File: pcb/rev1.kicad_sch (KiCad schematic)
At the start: 50 parts, among them SW1 SW_Push, SW10 SW_Push, SW11 SW_Push, SW12 SW_Push, SW13 SW_Push, SW14 SW_Push, SW15 SW_Push, SW16 SW_Push, SW2 SW_Push, SW3 SW_Push, SW4 SW_Push, SW5 SW_Push, SW6 SW_Push, SW7 SW_Push, SW8 SW_Push, SW9 SW_Push, U1 XIAO-RP2040-DIP, U2 OLED_0.91_128x32

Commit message: Fixed LED footprint
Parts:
- D1, D10, D11, D12, D13, D14, D15, D16, D2, D3, D4, D5, D6, D7, D8, D9: footprint LED_SMD:LED_SK6812_PLCC4_5.0x5.0mm_P3.2mm -> Hackclub symbols:MX_SK6812MINI-E_REV
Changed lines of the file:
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@@
 			)
 		)
-		(property "Footprint" "LED_SMD:LED_SK6812_PLCC4_5.0x5.0mm_P3.2mm"
+		(property "Footprint" "Hackclub symbols:MX_SK6812MINI-E_REV"
 			(at 67.31 128.27 0)
 			(effects
@@
 			)
 		)
-		(property "Footprint" "LED_SMD:LED_SK6812_PLCC4_5.0x5.0mm_P3.2mm"
+		(property "Footprint" "Hackclub symbols:MX_SK6812MINI-E_REV"
 			(at 102.87 146.05 0)
 			(effects
@@
 			)
 		)
-		(property "Footprint" "LED_SMD:LED_SK6812_PLCC4_5.0x5.0mm_P3.2mm"
+		(property "Footprint" "Hackclub symbols:MX_SK6812MINI-E_REV"
 			(at 85.09 146.05 0)
 			(effects
@@
 			)
 		)
-		(property "Footprint" "LED_SMD:LED_SK6812_PLCC4_5.0x5.0mm_P3.2mm"
+		(property "Footprint" "Hackclub symbols:MX_SK6812MINI-E_REV"
 			(at 120.65 146.05 0)
 			(effects
@@
 			)
 		)
-		(property "Footprint" "LED_SMD:LED_SK6812_PLCC4_5.0x5.0mm_P3.2mm"
+		(property "Footprint" "Hackclub symbols:MX_SK6812MINI-E_REV"
 			(at 120.65 128.27 0)
 			(effects
@@
 			)
 		)
-		(property "Footprint" "LED_SMD:LED_SK6812_PLCC4_5.0x5.0mm_P3.2mm"
+		(property "Footprint" "Hackclub symbols:MX_SK6812MINI-E_REV"
 			(at 102.87 163.83 0)
 			(effects
@@
 			)
 		)
-		(property "Footprint" "LED_SMD:LED_SK6812_PLCC4_5.0x5.0mm_P3.2mm"
+		(property "Footprint" "Hackclub symbols:MX_SK6812MINI-E_REV"
 			(at 85.09 110.49 0)
 			(effects
@@
 			)
 		)
-		(property "Footprint" "LED_SMD:LED_SK6812_PLCC4_5.0x5.0mm_P3.2mm"
+		(property "Footprint" "Hackclub symbols:MX_SK6812MINI-E_REV"
 			(at 67.31 110.49 0)
 			(effects
@@
 			)
 		)
-		(property "Footprint" "LED_SMD:LED_SK6812_PLCC4_5.0x5.0mm_P3.2mm"
+		(property "Footprint" "Hackclub symbols:MX_SK6812MINI-E_REV"
 			(at 120.65 110.49 0)
 			(effects
@@
 			)
 		)
-		(property "Footprint" "LED_SMD:LED_SK6812_PLCC4_5.0x5.0mm_P3.2mm"
+		(property "Footprint" "Hackclub symbols:MX_SK6812MINI-E_REV"
 			(at 67.31 163.83 0)
 			(effects
@@
 			)
 		)
-		(property "Footprint" "LED_SMD:LED_SK6812_PLCC4_5.0x5.0mm_P3.2mm"
+		(property "Footprint" "Hackclub symbols:MX_SK6812MINI-E_REV"
 			(at 102.87 128.27 0)
 			(effects
@@
 			)
 		)
-		(property "Footprint" "LED_SMD:LED_SK6812_PLCC4_5.0x5.0mm_P3.2mm"
+		(property "Footprint" "Hackclub symbols:MX_SK6812MINI-E_REV"
 			(at 102.87 110.49 0)
 			(effects
@@
 			)
 		)
-		(property "Footprint" "LED_SMD:LED_SK6812_PLCC4_5.0x5.0mm_P3.2mm"
+		(property "Footprint" "Hackclub symbols:MX_SK6812MINI-E_REV"
 			(at 85.09 163.83 0)
 			(effects
@@
 			)
 		)
-		(property "Footprint" "LED_SMD:LED_SK6812_PLCC4_5.0x5.0mm_P3.2mm"
+		(property "Footprint" "Hackclub symbols:MX_SK6812MINI-E_REV"
 			(at 85.09 128.27 0)
 			(effects
@@
 			)
 		)
-		(property "Footprint" "LED_SMD:LED_SK6812_PLCC4_5.0x5.0mm_P3.2mm"
+		(property "Footprint" "Hackclub symbols:MX_SK6812MINI-E_REV"
 			(at 67.31 146.05 0)
 			(effects
@@
 			)
 		)
-		(property "Footprint" "LED_SMD:LED_SK6812_PLCC4_5.0x5.0mm_P3.2mm"
+		(property "Footprint" "Hackclub symbols:MX_SK6812MINI-E_REV"
 			(at 120.65 163.83 0)
 			(effects

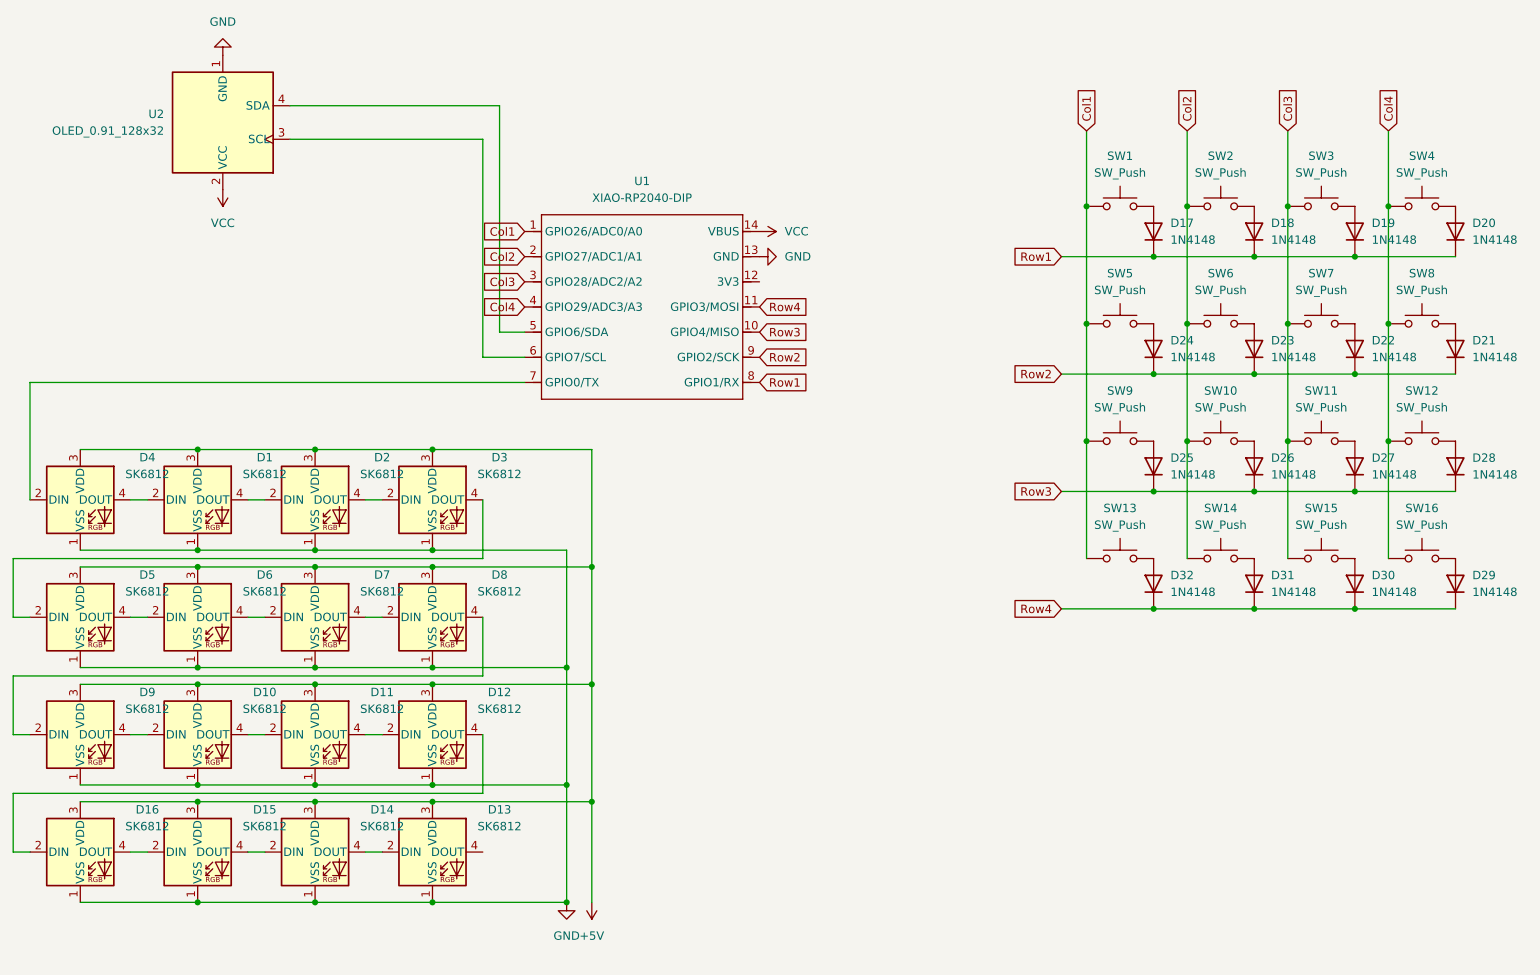
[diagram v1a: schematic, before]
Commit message: Fixed LEDs not getting power
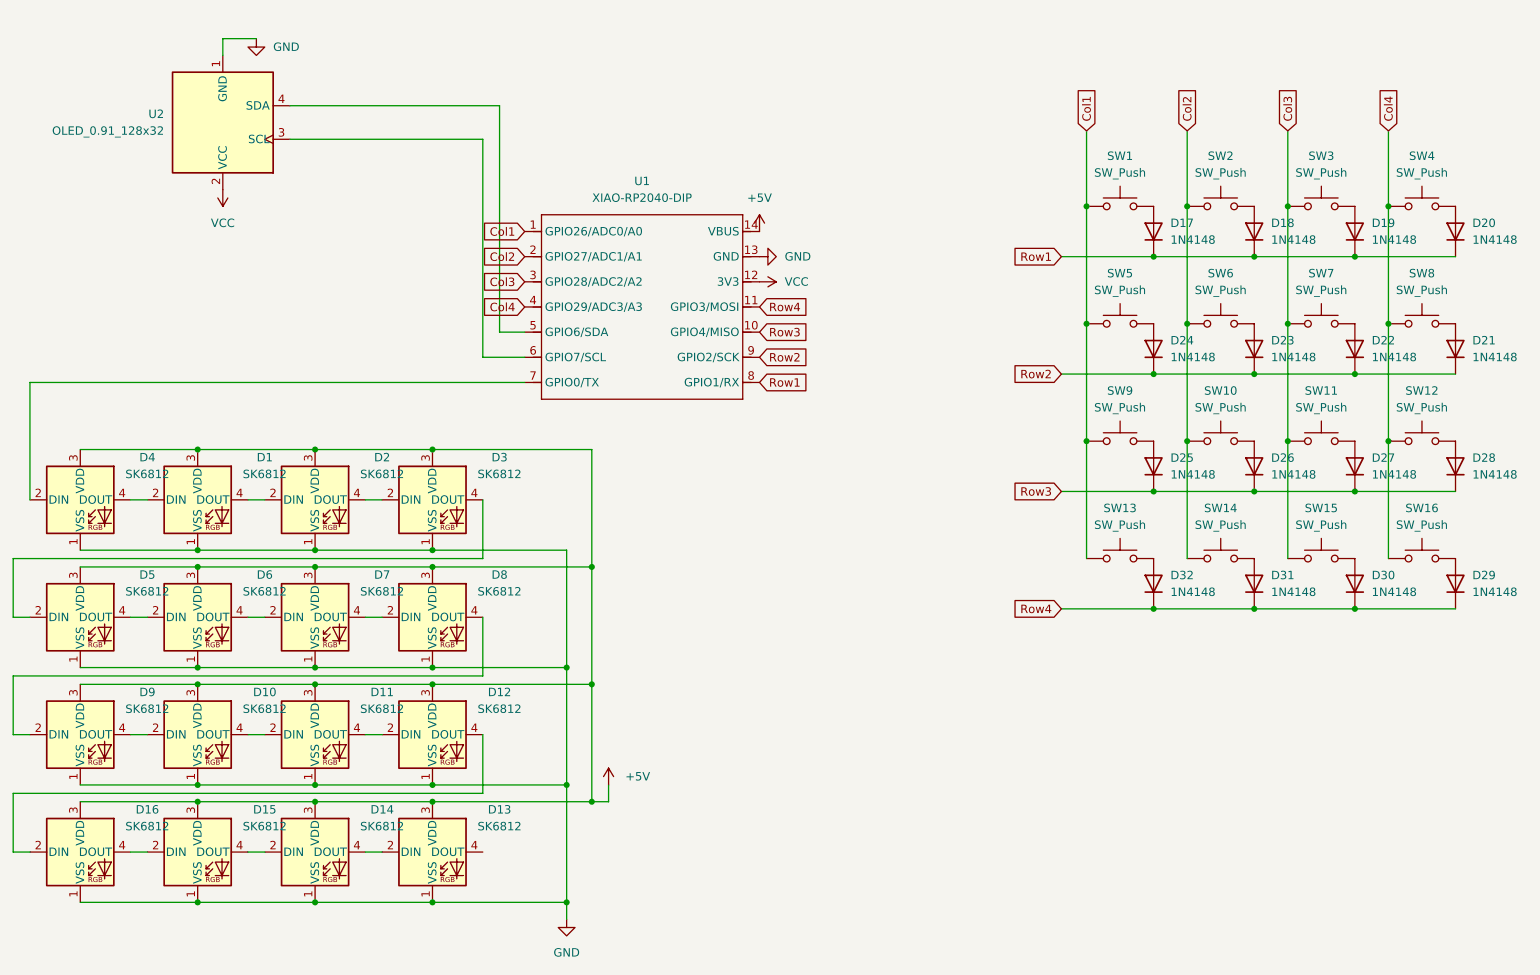
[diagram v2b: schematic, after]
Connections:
- net +5V: now also U1.14 (VBUS)
- net VCC: now also U1.12 (3V3); no longer U1.14 (VBUS)
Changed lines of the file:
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@@
 	)
 	(junction
-		(at 139.7 163.83)
-		(diameter 0)
-		(color 0 0 0 0)
-	)
-	(junction
 		(at 119.38 128.27)
 		(diameter 0)
@@
 	)
 	(junction
+		(at 139.7 163.83)
+		(diameter 0)
+		(color 0 0 0 0)
+	)
+	(junction
 		(at 119.38 110.49)
 		(diameter 0)
@@
 	(wire
 		(pts
+			(xy 146.05 148.59) (xy 143.51 148.59)
+		)
+		(stroke
+			(width 0)
+			(type default)
+		)
+	)
+	(wire
+		(pts
 			(xy 55.88 111.76) (xy 55.88 120.65)
 		)
@@
 	(wire
 		(pts
+			(xy 139.7 166.37) (xy 139.7 163.83)
+		)
+		(stroke
+			(width 0)
+			(type default)
+		)
+	)
+	(wire
+		(pts
 			(xy 101.6 128.27) (xy 83.82 128.27)
 		)
@@
 	(wire
 		(pts
+			(xy 92.71 33.02) (xy 87.63 33.02)
+		)
+		(stroke
+			(width 0)
+			(type default)
+		)
+	)
+	(wire
+		(pts
 			(xy 214.63 83.82) (xy 228.6 83.82)
 		)
@@
 	(wire
 		(pts
+			(xy 87.63 33.02) (xy 87.63 35.56)
+		)
+		(stroke
+			(width 0)
+			(type default)
+		)
+	)
+	(wire
+		(pts
 			(xy 127 102.87) (xy 127 111.76)
 		)
@@
 	(wire
 		(pts
-			(xy 143.51 163.83) (xy 143.51 148.59)
+			(xy 146.05 146.05) (xy 146.05 148.59)
 		)
 		(stroke
@@
 	(symbol
 		(lib_id "power:GND")
-		(at 139.7 163.83 0)
+		(at 139.7 166.37 0)
 		(unit 1)
 		(exclude_from_sim no)
@@
 		(fields_autoplaced yes)
 		(property "Reference" "#PWR03"
-			(at 139.7 170.18 0)
+			(at 139.7 172.72 0)
 			(effects
 				(font
@@
 		)
 		(property "Value" "GND"
-			(at 139.7 168.91 0)
+			(at 139.7 171.45 0)
 			(effects
 				(font
@@
 		)
 		(property "Footprint" ""
-			(at 139.7 163.83 0)
+			(at 139.7 166.37 0)
 			(effects
 				(font
@@
 		)
 		(property "Datasheet" ""
-			(at 139.7 163.83 0)
+			(at 139.7 166.37 0)
 			(effects
 				(font
@@
 		)
 		(property "Description" "Power symbol creates a global label with name \"GND\" , ground"
-			(at 139.7 163.83 0)
+			(at 139.7 166.37 0)
 			(effects
 				(font
@@
 	(symbol
 		(lib_id "power:VCC")
-		(at 168.91 62.23 270)
+		(at 168.91 69.85 270)
 		(unit 1)
 		(exclude_from_sim no)
@@
 		(fields_autoplaced yes)
 		(property "Reference" "#PWR05"
-			(at 165.1 62.23 0)
+			(at 165.1 69.85 0)
 			(effects
 				(font
@@
 		)
 		(property "Value" "VCC"
-			(at 172.72 62.2299 90)
+			(at 172.72 69.8499 90)
 			(effects
 				(font
@@
 		)
 		(property "Footprint" ""
-			(at 168.91 62.23 0)
+			(at 168.91 69.85 0)
 			(effects
 				(font
@@
 		)
 		(property "Datasheet" ""
-			(at 168.91 62.23 0)
+			(at 168.91 69.85 0)
 			(effects
 				(font
@@
 		)
 		(property "Description" "Power symbol creates a global label with name \"VCC\""
-			(at 168.91 62.23 0)
+			(at 168.91 69.85 0)
 			(effects
 				(font
@@
 	(symbol
 		(lib_id "power:+5V")
-		(at 143.51 163.83 180)
+		(at 146.05 146.05 0)
 		(unit 1)
 		(exclude_from_sim no)
@@
 		(fields_autoplaced yes)
 		(property "Reference" "#PWR04"
-			(at 143.51 160.02 0)
+			(at 146.05 149.86 0)
 			(effects
 				(font
@@
 		)
 		(property "Value" "+5V"
-			(at 143.51 168.91 0)
+			(at 148.59 144.7799 0)
 			(effects
 				(font
 					(size 1.27 1.27)
 				)
+				(justify left)
 			)
 		)
 		(property "Footprint" ""
-			(at 143.51 163.83 0)
+			(at 146.05 146.05 0)
 			(effects
 				(font
@@
 		)
 		(property "Datasheet" ""
-			(at 143.51 163.83 0)
+			(at 146.05 146.05 0)
 			(effects
 				(font
@@
 		)
 		(property "Description" "Power symbol creates a global label with name \"+5V\""
-			(at 143.51 163.83 0)
+			(at 146.05 146.05 0)
 			(effects
 				(font
@@
 	(symbol
 		(lib_id "power:GND")
-		(at 87.63 35.56 180)
+		(at 92.71 33.02 0)
 		(unit 1)
 		(exclude_from_sim no)
@@
 		(fields_autoplaced yes)
 		(property "Reference" "#PWR02"
-			(at 87.63 29.21 0)
+			(at 92.71 39.37 0)
 			(effects
 				(font
@@
 		)
 		(property "Value" "GND"
-			(at 87.63 30.48 0)
+			(at 95.25 34.2899 0)
 			(effects
 				(font
 					(size 1.27 1.27)
 				)
+				(justify left)
 			)
 		)
 		(property "Footprint" ""
-			(at 87.63 35.56 0)
+			(at 92.71 33.02 0)
 			(effects
 				(font
@@
 		)
 		(property "Datasheet" ""
-			(at 87.63 35.56 0)
+			(at 92.71 33.02 0)
 			(effects
 				(font
@@
 		)
 		(property "Description" "Power symbol creates a global label with name \"GND\" , ground"
-			(at 87.63 35.56 0)
+			(at 92.71 33.02 0)
 			(effects
 				(font
@@
 					(unit 1)
 				)
+			)
+		)
+	)
+	(symbol
+		(lib_id "power:+5V")
+		(at 168.91 62.23 0)
+		(unit 1)
+		(exclude_from_sim no)
+		(in_bom yes)
+		(on_board yes)
+		(dnp no)
+		(fields_autoplaced yes)
+		(property "Reference" "#PWR07"
+			(at 168.91 66.04 0)
+			(effects
+				(font
+					(size 1.27 1.27)
+				)
+				(hide yes)
+			)
+		)
+		(property "Value" "+5V"
+			(at 168.91 57.15 0)
+			(effects
+				(font
+					(size 1.27 1.27)
+				)
+			)
+		)
+		(property "Footprint" ""
+			(at 168.91 62.23 0)
+			(effects
+				(font
+					(size 1.27 1.27)
+				)
+				(hide yes)
+			)
+		)
+		(property "Datasheet" ""
+			(at 168.91 62.23 0)
+			(effects
+				(font
+					(size 1.27 1.27)
+				)
+				(hide yes)
+			)
+		)
+		(property "Description" "Power symbol creates a global label with name \"+5V\""
+			(at 168.91 62.23 0)
+			(effects
+				(font
+					(size 1.27 1.27)
+				)
+				(hide yes)
+			)
+		)
+		(pin "1"
+		)
+		(instances
+			(project ""
+				(path "/de3dff5d-dbe4-4551-99b2-98eb980878a0"
+					(reference "#PWR07")
+					(unit 1)
+				)
